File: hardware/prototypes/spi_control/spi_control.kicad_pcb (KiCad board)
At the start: 4 copper layers, 66.9 x 43.2 mm, 85 parts, among them J1 USB_B_Micro, J39 Versa_1, J40 Versa_2, U1 ST1L08SPU33R, U2 MCP2210-I_MQ, U3 ADAR7251, U4 BGT24_Module, Y1 12MHZ, Y2 40MHz

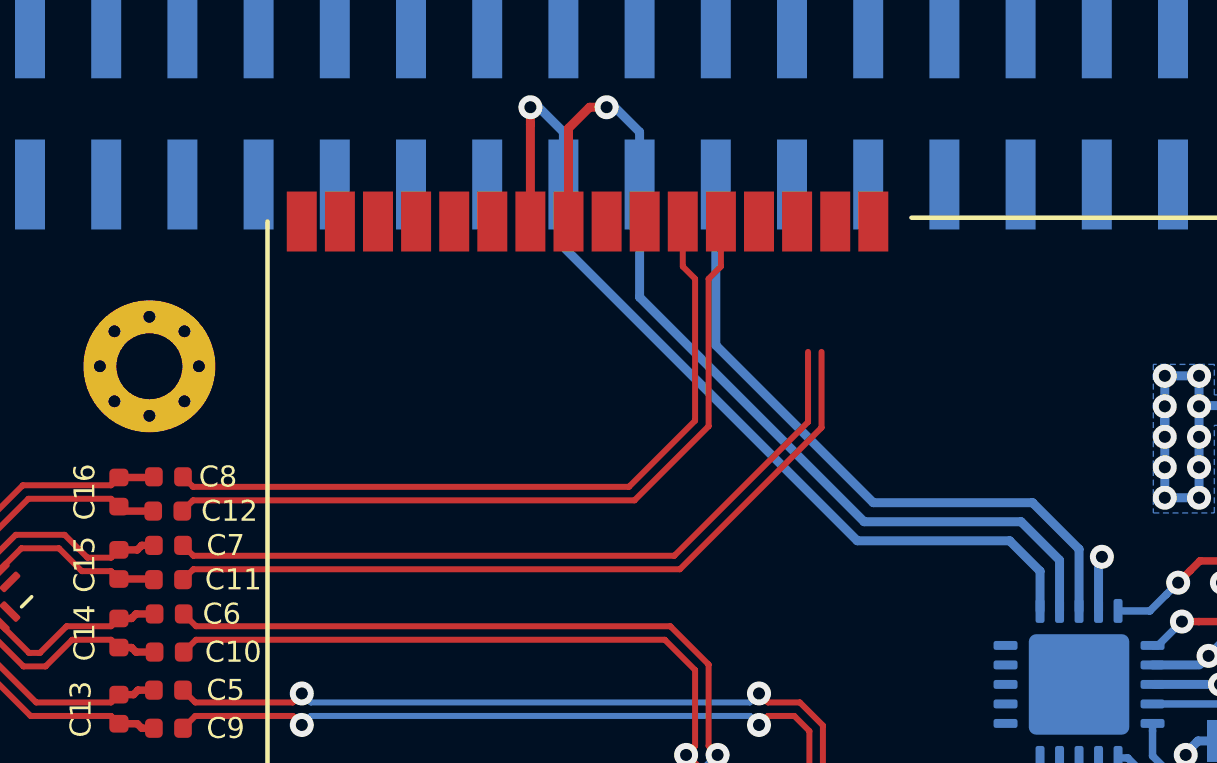
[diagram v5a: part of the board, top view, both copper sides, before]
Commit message: finished prelim IQ routing
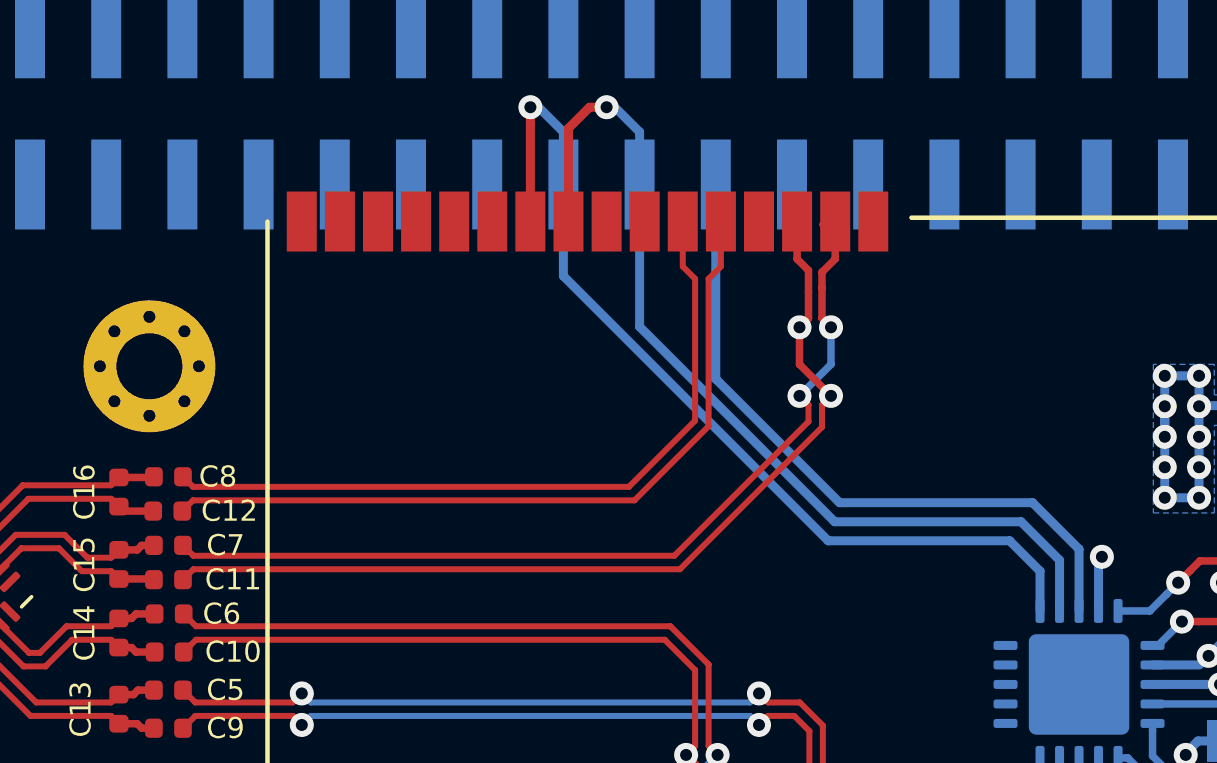
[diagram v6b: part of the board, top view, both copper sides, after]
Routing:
- net /IF2_Q-: track 25.2 -> 31.0 mm, vias 0 -> 2
- net /IF2_Q+: track 25.9 -> 31.7 mm, vias 0 -> 2
- net /PLL_RSET: track 22.3 -> 23.0 mm
- net /PLL_MUX: track 31.3 -> 31.9 mm
- net /PLL_MOD: track 31.2 -> 31.7 mm
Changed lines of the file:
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@@
     (thickness 1.6)
     (drawings 14)
-    (tracks 365)
+    (tracks 387)
     (zones 0)
     (modules 85)
@@
   (gr_line (start 124.333 56.261) (end 124.333 96.139) (layer Edge.Cuts) (width 0.05))
   (gr_line (start 59.055 54.61) (end 116.84 54.61) (layer Edge.Cuts) (width 0.05))
+  (segment (start 99.89 66.98) (end 100.19 67.28) (width 0.25) (layer F.Cu) (net 7))
+  (segment (start 100.3 63.446001) (end 99.89 63.856001) (width 0.2) (layer F.Cu) (net 7))
+  (segment (start 99.14 69.566) (end 100.19 68.516) (width 0.25) (layer B.Cu) (net 7))
+  (segment (start 100.19 68.516) (end 100.19 67.28) (width 0.25) (layer B.Cu) (net 7))
+  (via (at 99.14 69.566) (size 0.8) (drill 0.4) (layers F.Cu B.Cu) (net 7))
+  (via (at 100.19 67.28) (size 0.8) (drill 0.4) (layers F.Cu B.Cu) (net 7))
+  (segment (start 99.03 63.446001) (end 99.44 63.856001) (width 0.2) (layer F.Cu) (net 11))
+  (segment (start 99.44 66.98) (end 99.14 67.28) (width 0.25) (layer F.Cu) (net 11))
+  (segment (start 99.14 68.516) (end 99.14 67.28) (width 0.25) (layer F.Cu) (net 11))
+  (segment (start 100.19 69.566) (end 99.14 68.516) (width 0.25) (layer F.Cu) (net 11))
+  (via (at 99.14 67.28) (size 0.8) (drill 0.4) (layers F.Cu B.Cu) (net 11))
+  (via (at 100.19 69.566) (size 0.8) (drill 0.4) (layers F.Cu B.Cu) (net 11))
   (segment (start 112.4585 71.9455) (end 112.4585 72.9615) (width 0.3) (layer B.Cu) (net 4))
   (segment (start 111.3155 71.9455) (end 111.3155 72.9615) (width 0.3) (layer B.Cu) (net 4))
@@
   (segment (start 95.36 82.584) (end 95.36 83.82) (width 0.25) (layer B.Cu) (net 6))
   (segment (start 96.41 81.534) (end 95.36 82.584) (width 0.25) (layer B.Cu) (net 6))
-  (segment (start 99.425 70.4368) (end 99.425 68.1) (width 0.2) (layer F.Cu) (net 7))
-  (segment (start 94.9663 74.8955) (end 99.425 70.4368) (width 0.2) (layer F.Cu) (net 7))
-  (segment (start 78.9365 74.8955) (end 94.9663 74.8955) (width 0.2) (layer F.Cu) (net 7))
-  (segment (start 78.59 74.549) (end 78.9365 74.8955) (width 0.2) (layer F.Cu) (net 7))
+  (segment (start 99.89 65.444) (end 99.89 65.96) (width 0.25) (layer F.Cu) (net 7))
+  (segment (start 100.33 65.004) (end 99.89 65.444) (width 0.25) (layer F.Cu) (net 7))
+  (segment (start 100.33 63.754) (end 100.33 65.004) (width 0.25) (layer F.Cu) (net 7))
+  (segment (start 99.89 65.96) (end 99.89 66.98) (width 0.25) (layer F.Cu) (net 7))
+  (segment (start 94.9663 74.8955) (end 78.9365 74.8955) (width 0.2) (layer F.Cu) (net 7))
+  (segment (start 99.44 70.4218) (end 94.9663 74.8955) (width 0.2) (layer F.Cu) (net 7))
+  (segment (start 78.9365 74.8955) (end 78.59 74.549) (width 0.2) (layer F.Cu) (net 7))
+  (segment (start 99.44 69.866) (end 99.44 70.4218) (width 0.2) (layer F.Cu) (net 7))
+  (segment (start 99.14 69.566) (end 99.44 69.866) (width 0.2) (layer F.Cu) (net 7))
   (segment (start 78.925 72.598) (end 93.4538 72.598) (width 0.2) (layer F.Cu) (net 8))
   (segment (start 78.59 72.263) (end 78.925 72.598) (width 0.2) (layer F.Cu) (net 8))
@@
   (segment (start 96.41 82.584) (end 96.41 83.82) (width 0.25) (layer F.Cu) (net 10))
   (segment (start 95.36 81.534) (end 96.41 82.584) (width 0.25) (layer F.Cu) (net 10))
-  (segment (start 95.1527 75.3455) (end 99.875 70.6232) (width 0.2) (layer F.Cu) (net 11))
-  (segment (start 78.59 75.692) (end 78.9365 75.3455) (width 0.2) (layer F.Cu) (net 11))
-  (segment (start 99.875 70.6232) (end 99.875 68.1) (width 0.2) (layer F.Cu) (net 11))
-  (segment (start 78.9365 75.3455) (end 95.1527 75.3455) (width 0.2) (layer F.Cu) (net 11))
+  (segment (start 99.44 65.384) (end 99.44 66.11) (width 0.25) (layer F.Cu) (net 11))
+  (segment (start 99.06 65.004) (end 99.44 65.384) (width 0.25) (layer F.Cu) (net 11))
+  (segment (start 99.06 63.754) (end 99.06 65.004) (width 0.25) (layer F.Cu) (net 11))
+  (segment (start 99.44 66.11) (end 99.44 66.98) (width 0.25) (layer F.Cu) (net 11))
+  (segment (start 78.9365 75.3455) (end 78.59 75.692) (width 0.2) (layer F.Cu) (net 11))
+  (segment (start 100.19 69.566) (end 99.89 69.866) (width 0.2) (layer F.Cu) (net 11))
+  (segment (start 99.89 69.866) (end 99.89 70.6082) (width 0.2) (layer F.Cu) (net 11))
+  (segment (start 99.89 70.6082) (end 95.1527 75.3455) (width 0.2) (layer F.Cu) (net 11))
+  (segment (start 95.1527 75.3455) (end 78.9365 75.3455) (width 0.2) (layer F.Cu) (net 11))
   (segment (start 78.567 73.406) (end 78.925 73.048) (width 0.2) (layer F.Cu) (net 12))
   (segment (start 78.925 73.048) (end 93.6402 73.048) (width 0.2) (layer F.Cu) (net 12))
@@
   (segment (start 110.49 83.081) (end 110.49 82.042) (width 0.25) (layer B.Cu) (net 33))
   (segment (start 110.49 82.042) (end 110.0825 81.6345) (width 0.25) (layer B.Cu) (net 33))
-  (segment (start 96.35 67.8766) (end 96.35 62.52) (width 0.3) (layer B.Cu) (net 42))
-  (segment (start 101.6 73.1266) (end 96.35 67.8766) (width 0.3) (layer B.Cu) (net 42))
-  (segment (start 106.9086 73.1266) (end 101.6 73.1266) (width 0.3) (layer B.Cu) (net 42))
+  (segment (start 96.35 69) (end 96.35 62.52) (width 0.3) (layer B.Cu) (net 42))
+  (segment (start 100.4766 73.1266) (end 96.35 69) (width 0.3) (layer B.Cu) (net 42))
+  (segment (start 106.9086 73.1266) (end 100.4766 73.1266) (width 0.3) (layer B.Cu) (net 42))
   (segment (start 108.458 76.7345) (end 108.458 74.676) (width 0.3) (layer B.Cu) (net 42))
   (segment (start 108.458 74.676) (end 106.9086 73.1266) (width 0.3) (layer B.Cu) (net 42))
@@
   (segment (start 107.808 75.042) (end 107.808 76.7345) (width 0.3) (layer B.Cu) (net 43))
   (segment (start 106.5276 73.7616) (end 107.808 75.042) (width 0.3) (layer B.Cu) (net 43))
-  (segment (start 101.2952 73.7616) (end 106.5276 73.7616) (width 0.3) (layer B.Cu) (net 43))
-  (segment (start 93.81 62.52) (end 93.81 66.2764) (width 0.3) (layer B.Cu) (net 43))
-  (segment (start 93.81 66.2764) (end 101.2952 73.7616) (width 0.3) (layer B.Cu) (net 43))
+  (segment (start 100.3116 73.7616) (end 106.5276 73.7616) (width 0.3) (layer B.Cu) (net 43))
+  (segment (start 93.81 62.52) (end 93.81 67.26) (width 0.3) (layer B.Cu) (net 43))
+  (segment (start 93.81 67.26) (end 100.3116 73.7616) (width 0.3) (layer B.Cu) (net 43))
   (via (at 90.17 59.944) (size 0.8) (drill 0.4) (layers F.Cu B.Cu) (net 44))
   (segment (start 90.444 59.944) (end 90.17 59.944) (width 0.3) (layer B.Cu) (net 44))
@@
   (segment (start 90.17 60.509685) (end 90.17 64.135) (width 0.3) (layer F.Cu) (net 44))
   (segment (start 90.17 59.944) (end 90.17 60.509685) (width 0.3) (layer F.Cu) (net 44))
-  (segment (start 91.27 64.6) (end 91.27 62.52) (width 0.3) (layer B.Cu) (net 44))
-  (segment (start 101.0666 74.3966) (end 91.27 64.6) (width 0.3) (layer B.Cu) (net 44))
-  (segment (start 106.1466 74.3966) (end 101.0666 74.3966) (width 0.3) (layer B.Cu) (net 44))
+  (segment (start 91.27 65.57) (end 91.27 62.52) (width 0.3) (layer B.Cu) (net 44))
+  (segment (start 100.0966 74.3966) (end 91.27 65.57) (width 0.3) (layer B.Cu) (net 44))
+  (segment (start 106.1466 74.3966) (end 100.0966 74.3966) (width 0.3) (layer B.Cu) (net 44))
   (segment (start 107.158 76.7345) (end 107.158 75.408) (width 0.3) (layer B.Cu) (net 44))
   (segment (start 107.158 75.408) (end 106.1466 74.3966) (width 0.3) (layer B.Cu) (net 44))

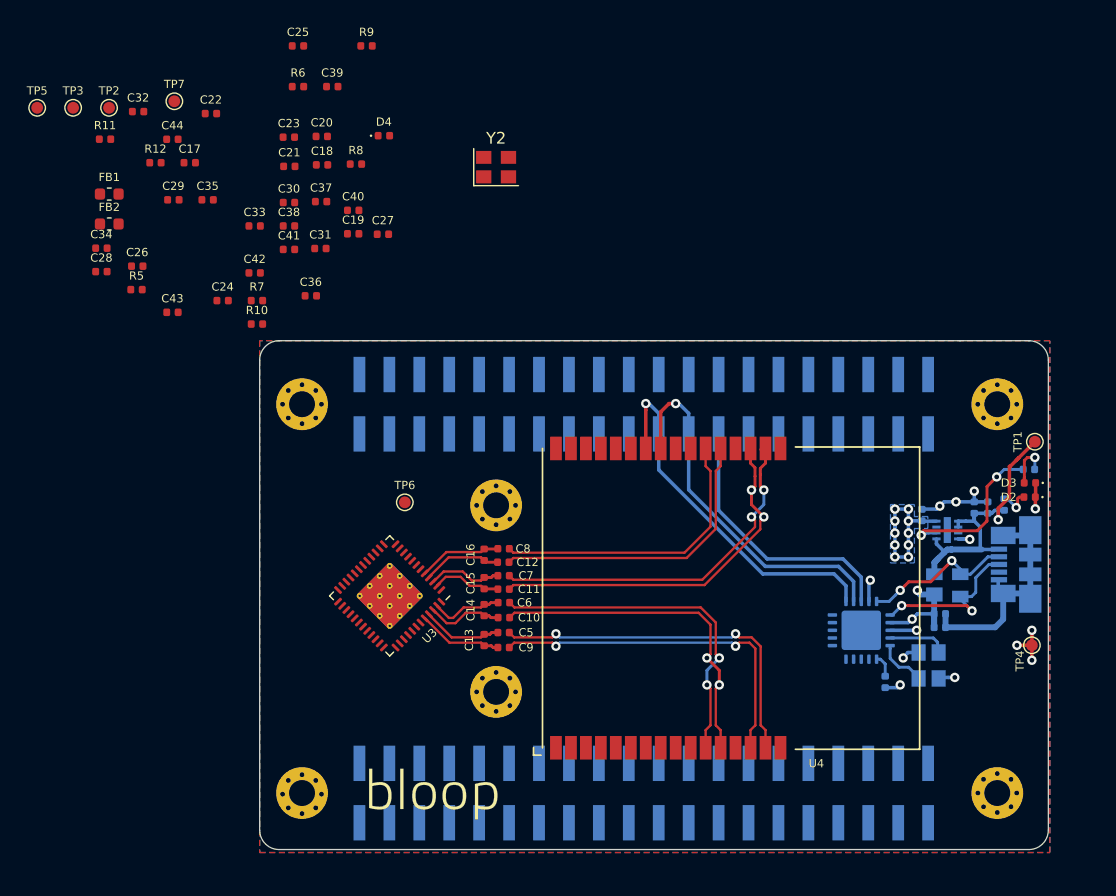
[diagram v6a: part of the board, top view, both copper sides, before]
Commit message: Completed power section, completed analog power and gnd plane,fixed IQ lines to be symmetric, ADC 80% routing completed.
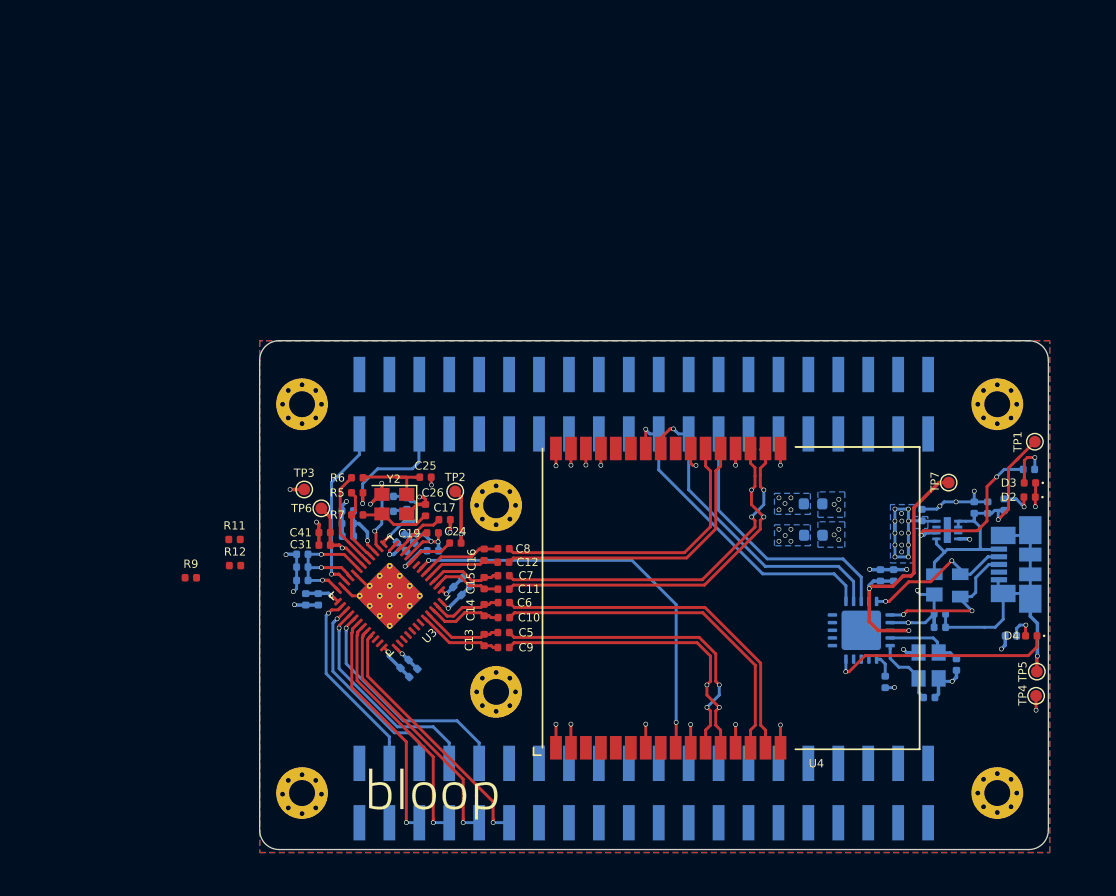
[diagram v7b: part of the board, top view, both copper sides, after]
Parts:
- C18, C20, C21, C22, C23, C27, C28, C29, C30, C32, C33, C34, C35, C36, C37, C38, C39, C40, C42, C43, C44, FB1, FB2, R10, R8: moved to B.Cu
- moved TP5 97.4 mm to (123.4, 82.7), turned to 270 degrees
- moved TP7 73.2 mm to (115.9, 66.6), turned to 90 degrees
- moved C23 72.2 mm to (114.2, 84.9), turned to 180 degrees
- moved C21 70.7 mm to (116.5, 82.1), turned to 90 degrees
- moved D4 69.4 mm to (122.9, 79.7), turned to 180 degrees
- moved R8 68.5 mm to (121.2, 79.7)
- moved FB1 66.4 mm to (104.4, 71.1)
- moved FB2 64.3 mm to (104.4, 68.5)
- moved C20 61.2 mm to (111.2, 74.5), turned to 90 degrees
- moved C18 58.8 mm to (110.1, 74.5), turned to 90 degrees
- moved R9 47.5 mm to (51.6, 74.7)
- moved C32 44.1 mm to (62.4, 76.6), turned to 270 degrees
- moved TP2 43.8 mm to (74.0, 67.4), turned to 90 degrees
- moved C22 41.6 mm to (72.1, 72.4)
- moved C39 40.8 mm to (61.0, 73.8), turned to 180 degrees
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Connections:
- C10 pad 1: /IF1_I+ -> /IF1_Q+
- C10 pad 2: /F_IF1_I+ -> /F_IF1_Q+
- C13 pad 1: /F_IF1_Q- -> /F_IF1_I-
- C13 pad 2: /F_IF1_Q+ -> /F_IF1_I+
- C14 pad 1: /F_IF1_I- -> /F_IF1_Q-
- C14 pad 2: /F_IF1_I+ -> /F_IF1_Q+
- C5 pad 1: /IF1_Q- -> /IF1_I-
- C5 pad 2: /F_IF1_Q- -> /F_IF1_I-
- C6 pad 1: /IF1_I- -> /IF1_Q-
- C6 pad 2: /F_IF1_I- -> /F_IF1_Q-
- C9 pad 1: /IF1_Q+ -> /IF1_I+
- C9 pad 2: /F_IF1_Q+ -> /F_IF1_I+
- J39 pad 10: /ADC_DOUT4 -> /ADC_DOUT3
- J39 pad 11: /MISO -> /ADC_DOUT7
- J39 pad 12: /ADC_DOUT3 -> /MISO
- J39 pad 14: /ADC_DOUT2 -> /MOSI
- J39 pad 16: /ADC_DOUT1 -> /SCK
- J39 pad 18: /ADC_DOUT0 -> /SCLK_ADC
- J39 pad 4: /ADC_DOUT7 -> /ADC_DOUT0
- J39 pad 5: /SCLK_ADC -> /ADC_DOUT4
- J39 pad 6: /ADC_DOUT6 -> /ADC_DOUT1
- J39 pad 7: /SCK -> /ADC_DOUT5
- J39 pad 8: /ADC_DOUT5 -> /ADC_DOUT2
- J39 pad 9: /MOSI -> /ADC_DOUT6
- U3 pad 44: /F_IF1_Q+ -> /F_IF1_I+
- U3 pad 45: /F_IF1_Q- -> /F_IF1_I-
- U3 pad 46: /F_IF1_I+ -> /F_IF1_Q+
- U3 pad 47: /F_IF1_I- -> /F_IF1_Q-
- Y2 pad 1: Net-(C26-Pad2) -> Net-(C25-Pad2)
- Y2 pad 3: Net-(C25-Pad2) -> Net-(C26-Pad2)
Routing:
- net GNDA: track 0.00 -> 39.7 mm, vias 0 -> 22
- net /BGT24_ANA: track 0.00 -> 35.8 mm, vias 0 -> 2
- net GND: track 27.3 -> 55.4 mm, vias 12 -> 24
- net +3V3: track 19.1 -> 46.7 mm, vias 13 -> 24
- net +3.3VA: track 0.00 -> 23.7 mm, vias 0 -> 12
- net /ADC_DOUT7: track 0.00 -> 21.8 mm, vias 0 -> 1
- net /ADC_DOUT6: track 0.00 -> 21.3 mm, vias 0 -> 1
- net /ADC_DOUT5: track 0.00 -> 20.9 mm, vias 0 -> 1
- net /ADC_DOUT4: track 0.00 -> 20.3 mm, vias 0 -> 1
- net /ADC_DOUT3: track 0.00 -> 20.1 mm, vias 0 -> 1
- net /SPI_XFR: track 0.00 -> 19.1 mm, vias 0 -> 1
- net /ADC_DOUT2: track 0.00 -> 18.7 mm, vias 0 -> 1
- net /ADC_DOUT1: track 0.00 -> 17.3 mm, vias 0 -> 1
- net /ADC_DOUT0: track 0.00 -> 16.5 mm, vias 0 -> 1
- net /DATA_READY: track 0.00 -> 14.5 mm, vias 0 -> 1
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- added copper zone on B.Cu, net +3.3VA
- added copper zone on In2.Cu, net +3.3VA
- added copper zone on B.Cu, net GND
- added copper zone on B.Cu, net GNDA
- added copper zone on In1.Cu, net GNDA
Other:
- net class Default: via_dia 0.8 -> 0.4; via_drill 0.4 -> 0.3
- net class Power: via_dia 0.8 -> 0.4; via_drill 0.4 -> 0.3
